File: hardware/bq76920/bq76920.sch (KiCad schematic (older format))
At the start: 10 parts, among them J1 BAT+, J2 Conn_01x06, J3 therm, J4 boot_switch, J5 BAT-, J6 PACK+, J7 PACK-, J8 mcu interface

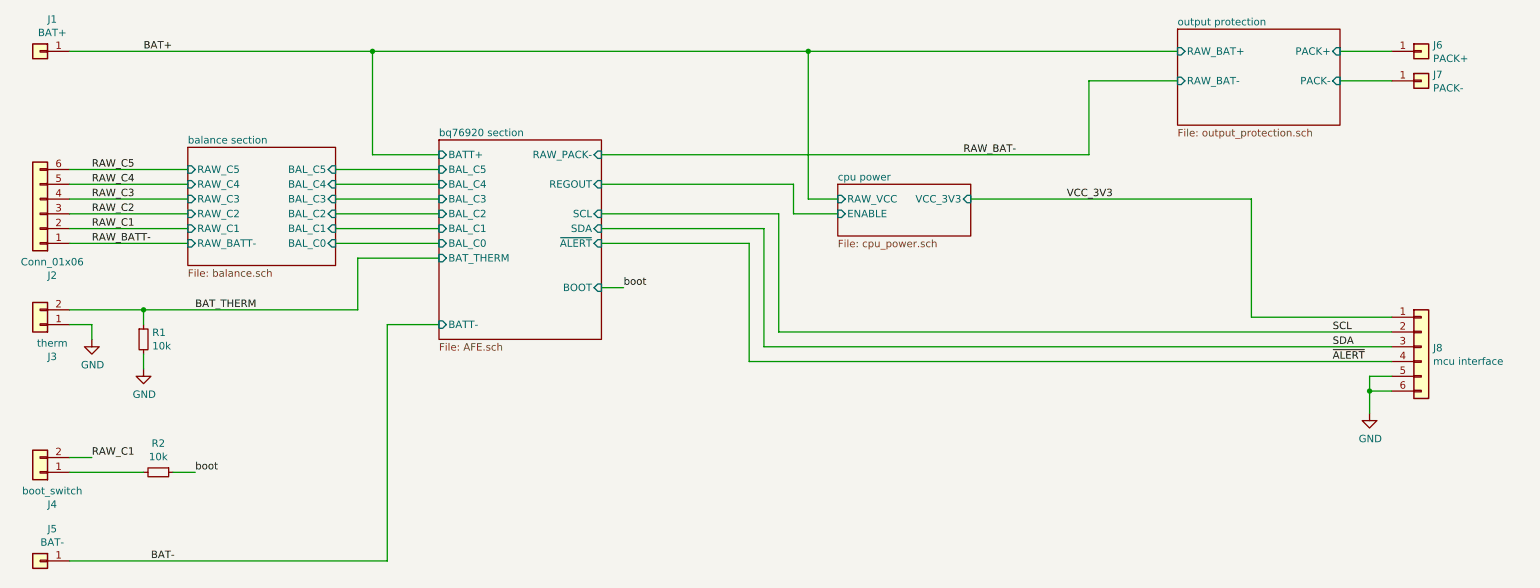
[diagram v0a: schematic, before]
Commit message: remove old project data
Signed-off-by: Ene Alexandru <ene.alexandru@gmail.com>
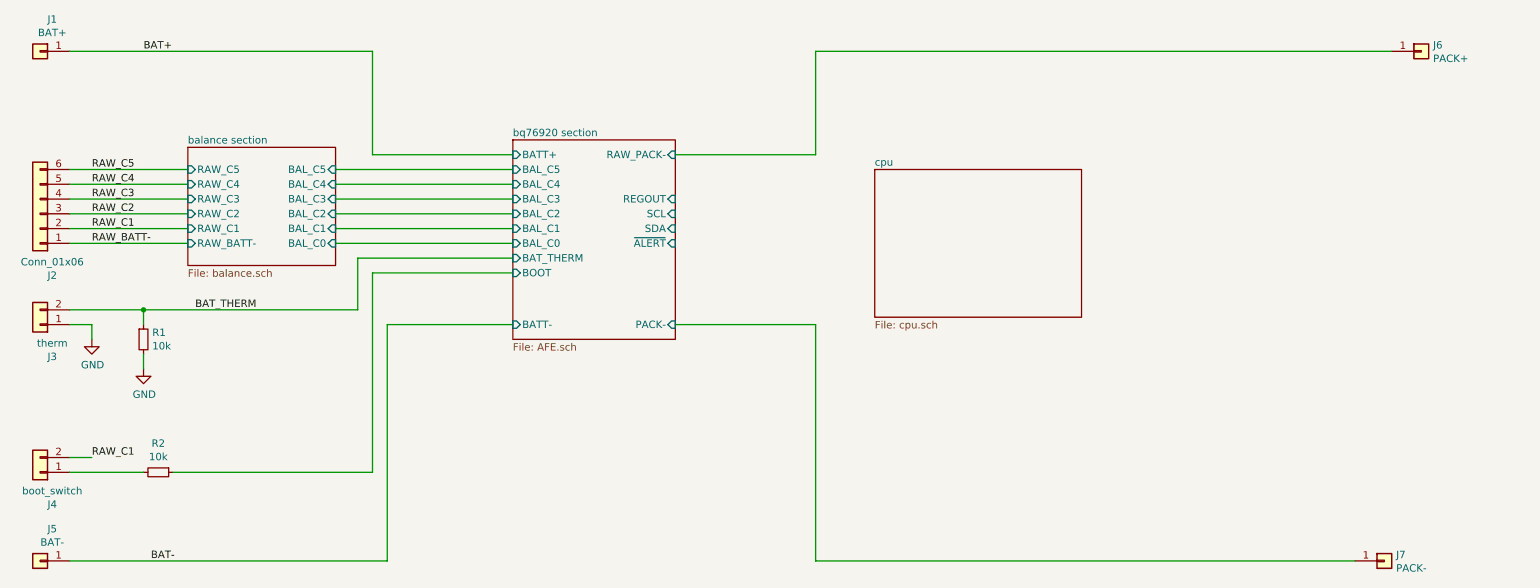
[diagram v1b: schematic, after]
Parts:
- removed J8: mcu interface, Connector_JST:JST_PH_B6B-PH-K_1x06_P2.00mm_Vertical, symbol Connector_Generic:Conn_01x06
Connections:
- net boot renamed bq76920 section/BOOT
- net output protection/PACK+ renamed bq76920 section/RAW_PACK-
- net output protection/PACK- renamed bq76920 section/PACK-
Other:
- moved on the sheet: J7
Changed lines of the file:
@@
 $Descr A4 11693 8268
 encoding utf-8
-Sheet 1 5
+Sheet 1 4
 Title ""
 Date ""
@@
 $EndDescr
 $Sheet
-S 3500 1500 1100 1350
+S 4000 1500 1100 1350
 U 5D32E153
 F0 "bq76920 section" 50
 F1 "AFE.sch" 50
-F2 "BAL_C5" I L 3500 1700 50
-F3 "BAL_C4" I L 3500 1800 50
-F4 "BAL_C3" I L 3500 1900 50
-F5 "BAL_C2" I L 3500 2000 50
-F6 "BAL_C1" I L 3500 2100 50
-F7 "BAL_C0" I L 3500 2200 50
-F8 "BATT-" I L 3500 2750 50
-F9 "~ALERT" I R 4600 2200 50
-F10 "BATT+" I L 3500 1600 50
-F11 "SCL" I R 4600 2000 50
-F12 "SDA" I R 4600 2100 50
-F13 "BOOT" I R 4600 2500 50
-F14 "BAT_THERM" I L 3500 2300 50
-F15 "REGOUT" I R 4600 1800 50
-F16 "RAW_PACK-" I R 4600 1600 50
+F2 "BAL_C5" I L 4000 1700 50
+F3 "BAL_C4" I L 4000 1800 50
+F4 "BAL_C3" I L 4000 1900 50
+F5 "BAL_C2" I L 4000 2000 50
+F6 "BAL_C1" I L 4000 2100 50
+F7 "BAL_C0" I L 4000 2200 50
+F8 "BATT-" I L 4000 2750 50
+F9 "~ALERT" I R 5100 2200 50
+F10 "BATT+" I L 4000 1600 50
+F11 "SCL" I R 5100 2000 50
+F12 "SDA" I R 5100 2100 50
+F13 "BOOT" I L 4000 2400 50
+F14 "BAT_THERM" I L 4000 2300 50
+F15 "REGOUT" I R 5100 1900 50
+F16 "RAW_PACK-" I R 5100 1600 50
+F17 "PACK-" I R 5100 2750 50
 $EndSheet
 $Sheet
@@
 	-1   0    0    -1
 $EndComp
-Wire Wire Line
-	2800 1700 3500 1700
-Wire Wire Line
-	3500 1800 2800 1800
-Wire Wire Line
-	2800 1900 3500 1900
-Wire Wire Line
-	3500 2000 2800 2000
-Wire Wire Line
-	2800 2100 3500 2100
-Wire Wire Line
-	3500 2200 2800 2200
 $Comp
 L Connector_Generic:Conn_01x02 J3
@@
 Wire Wire Line
 	2950 2300 2950 2650
-Wire Wire Line
-	2950 2300 3500 2300
-Wire Wire Line
-	3150 2750 3500 2750
-$Sheet
-S 8500 750  1100 650
-U 5D5964BC
-F0 "output protection" 50
-F1 "output_protection.sch" 50
-F2 "RAW_BAT+" I L 8500 900 50
-F3 "RAW_BAT-" I L 8500 1100 50
-F4 "PACK+" I R 9600 900 50
-F5 "PACK-" I R 9600 1100 50
-$EndSheet
 $Comp
 L Connector_Generic:Conn_01x01 J6
@@
 L Connector_Generic:Conn_01x01 J7
 U 1 1 5D59CAFF
-P 10150 1100
-F 0 "J7" H 10230 1142 50  0000 L CNN
-F 1 "PACK-" H 10230 1051 50  0000 L CNN
-F 2 "bq76920:power_pin" H 10150 1100 50  0001 C CNN
-F 3 "~" H 10150 1100 50  0001 C CNN
-	1    10150 1100
-	1    0    0    -1
-$EndComp
-Wire Wire Line
-	9600 900  9950 900
-$Sheet
-S 6200 1800 900  350
-U 5D59E152
-F0 "cpu power" 50
-F1 "cpu_power.sch" 50
-F2 "ENABLE" I L 6200 2000 50
-F3 "RAW_VCC" I L 6200 1900 50
-F4 "VCC_3V3" I R 7100 1900 50
-$EndSheet
-Wire Wire Line
-	9950 1100 9600 1100
+P 9900 4350
+F 0 "J7" H 9980 4392 50  0000 L CNN
+F 1 "PACK-" H 9980 4301 50  0000 L CNN
+F 2 "bq76920:power_pin" H 9900 4350 50  0001 C CNN
+F 3 "~" H 9900 4350 50  0001 C CNN
+	1    9900 4350
+	1    0    0    -1
+$EndComp
 Wire Wire Line
 	1000 900  3050 900
-Wire Wire Line
-	7900 1600 7900 1100
-Wire Wire Line
-	7900 1100 8500 1100
-Wire Wire Line
-	4600 1600 7900 1600
-Wire Wire Line
-	6200 1900 6000 1900
-Wire Wire Line
-	6000 1900 6000 900
-Connection ~ 6000 900
-Wire Wire Line
-	6000 900  8500 900
-Wire Wire Line
-	4600 1800 5900 1800
-Wire Wire Line
-	5900 1800 5900 2000
-Wire Wire Line
-	5900 2000 6200 2000
-Wire Wire Line
-	3150 2750 3150 4350
 $Comp
 L Device:R_Small R1
@@
 	-1   0    0    1
 $EndComp
-Text Label 4750 2500 0    50   ~ 0
-boot
-Wire Wire Line
-	4750 2500 4600 2500
-Text Label 1850 3750 0    50   ~ 0
-boot
 Text Label 1150 2100 0    50   ~ 0
 RAW_C1
@@
 $EndComp
 Wire Wire Line
-	1700 3750 1850 3750
-Wire Wire Line
 	1000 3750 1500 3750
-$Comp
-L Connector_Generic:Conn_01x06 J8
-U 1 1 5D5E72CD
-P 10150 2900
-F 0 "J8" H 10230 2892 50  0000 L CNN
-F 1 "mcu interface" H 10230 2801 50  0000 L CNN
-F 2 "Connector_JST:JST_PH_B6B-PH-K_1x06_P2.00mm_Vertical" H 10150 2900 50  0001 C CNN
-F 3 "~" H 10150 2900 50  0001 C CNN
-	1    10150 2900
-	1    0    0    -1
-$EndComp
-Wire Wire Line
-	9950 2700 9000 2700
-Wire Wire Line
-	9000 2700 9000 1900
-Wire Wire Line
-	9000 1900 7100 1900
-Wire Wire Line
-	4600 2000 5800 2000
-Wire Wire Line
-	5800 2000 5800 2800
-Wire Wire Line
-	5800 2800 9950 2800
-Wire Wire Line
-	9950 2900 5700 2900
-Wire Wire Line
-	5700 2900 5700 2100
-Wire Wire Line
-	5700 2100 4600 2100
-Wire Wire Line
-	9950 3000 5600 3000
-Wire Wire Line
-	5600 3000 5600 2200
-Wire Wire Line
-	5600 2200 4600 2200
-$Comp
-L power:GND #PWR03
-U 1 1 5D5EC925
-P 9800 3350
-F 0 "#PWR03" H 9800 3100 50  0001 C CNN
-F 1 "GND" H 9805 3177 50  0000 C CNN
-F 2 "" H 9800 3350 50  0001 C CNN
-F 3 "" H 9800 3350 50  0001 C CNN
-	1    9800 3350
-	1    0    0    -1
-$EndComp
-Wire Wire Line
-	9800 3350 9800 3200
-Wire Wire Line
-	9800 3100 9950 3100
-Wire Wire Line
-	9950 3200 9800 3200
-Connection ~ 9800 3200
-Wire Wire Line
-	9800 3200 9800 3100
 Wire Wire Line
 	1000 4350 3150 4350
 Wire Wire Line
-	3500 1600 3050 1600
-Wire Wire Line
 	3050 1600 3050 900
-Connection ~ 3050 900
-Wire Wire Line
-	3050 900  6000 900
 Text Label 1500 900  0    50   ~ 0
 BAT+
@@
 Text Label 1550 4350 0    50   ~ 0
 BAT-
-Text Label 7050 1600 0    50   ~ 0
-RAW_BAT-
-Text Label 7750 1900 0    50   ~ 0
-VCC_3V3
-Text Label 9550 2800 0    50   ~ 0
-SCL
-Text Label 9550 2900 0    50   ~ 0
-SDA
-Text Label 9550 3000 0    50   ~ 0
-~ALERT
+Wire Wire Line
+	3050 1600 4000 1600
+Wire Wire Line
+	2800 1700 4000 1700
+Wire Wire Line
+	2800 1800 4000 1800
+Wire Wire Line
+	2800 1900 4000 1900
+Wire Wire Line
+	2800 2000 4000 2000
+Wire Wire Line
+	2800 2100 4000 2100
+Wire Wire Line
+	2800 2200 4000 2200
+Wire Wire Line
+	2950 2300 4000 2300
+Wire Wire Line
+	3050 3750 3050 2400
+Wire Wire Line
+	3050 2400 4000 2400
+Wire Wire Line
+	1700 3750 3050 3750
+Wire Wire Line
+	4000 2750 3150 2750
+Wire Wire Line
+	3150 2750 3150 4350
+Wire Wire Line
+	5100 1600 6050 1600
+Wire Wire Line
+	6050 1600 6050 900
+Wire Wire Line
+	6050 900  9950 900
+Wire Wire Line
+	5100 2750 6050 2750
+Wire Wire Line
+	6050 2750 6050 4350
+Wire Wire Line
+	6050 4350 9700 4350
+$Sheet
+S 6450 1700 1400 1000
+U 5E142913
+F0 "cpu" 50
+F1 "cpu.sch" 50
+$EndSheet
 $EndSCHEMATC

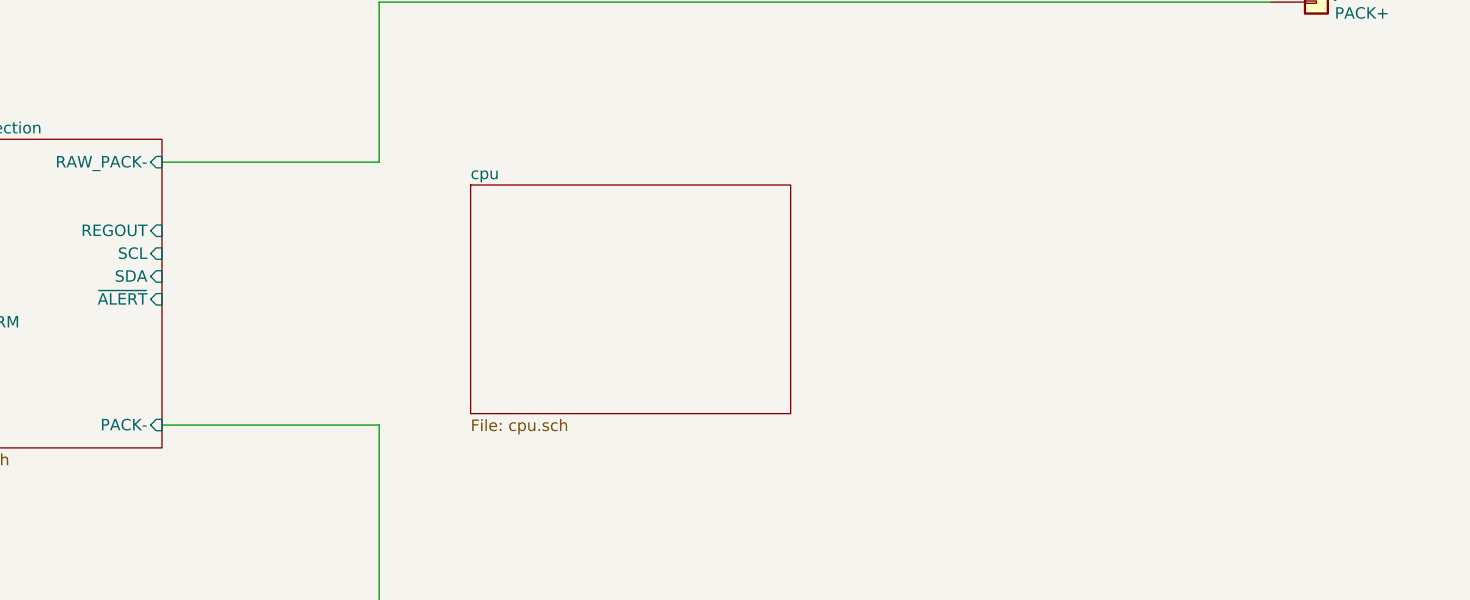
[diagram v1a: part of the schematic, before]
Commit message: update cpu and reduce BOM
Signed-off-by: Ene Alexandru <ene.alexandru@gmail.com>
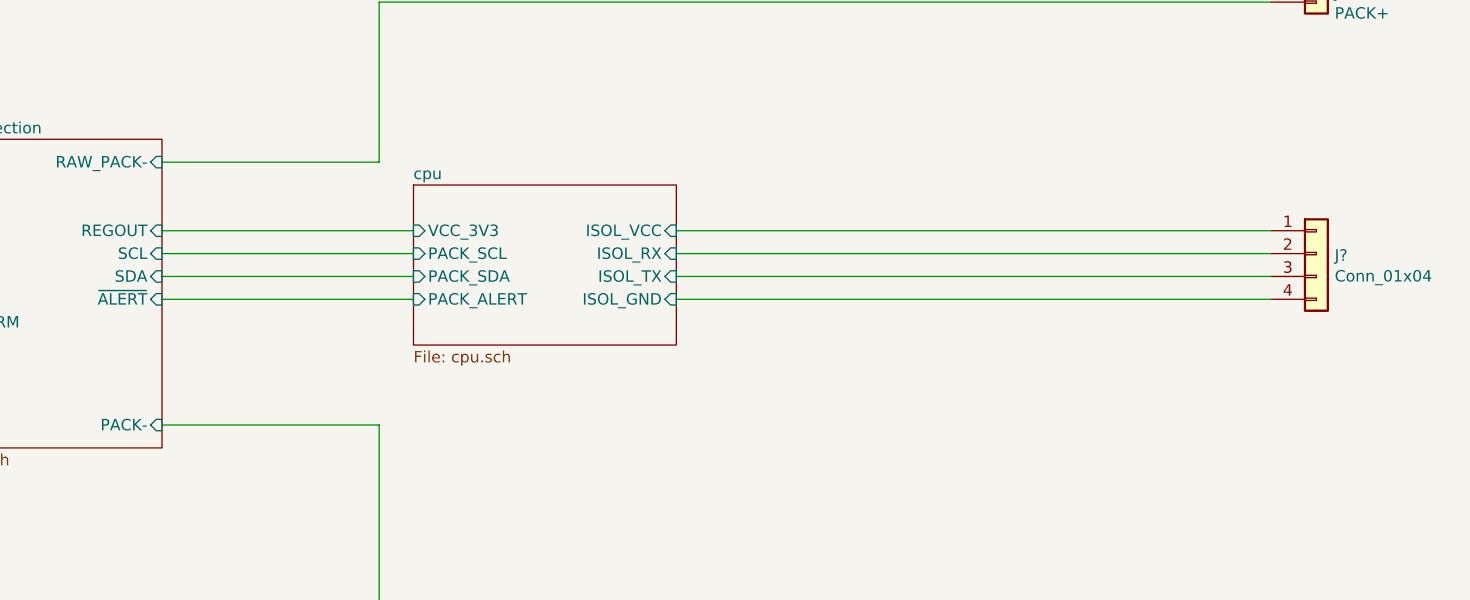
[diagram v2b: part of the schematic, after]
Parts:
- added J?: Conn_01x04, symbol Connector_Generic:Conn_01x04
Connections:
- new net cpu/ISOL_GND: J?.4 (Pin_4)
- new net cpu/ISOL_RX: J?.2 (Pin_2)
- new net cpu/ISOL_TX: J?.3 (Pin_3)
- new net cpu/ISOL_VCC: J?.1 (Pin_1)
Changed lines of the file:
@@
 	6050 4350 9700 4350
 $Sheet
-S 6450 1700 1400 1000
+S 6200 1700 1150 700
 U 5E142913
 F0 "cpu" 50
 F1 "cpu.sch" 50
+F2 "VCC_3V3" I L 6200 1900 50
+F3 "PACK_SCL" I L 6200 2000 50
+F4 "PACK_SDA" I L 6200 2100 50
+F5 "PACK_ALERT" I L 6200 2200 50
+F6 "ISOL_VCC" I R 7350 1900 50
+F7 "ISOL_RX" I R 7350 2000 50
+F8 "ISOL_TX" I R 7350 2100 50
+F9 "ISOL_GND" I R 7350 2200 50
 $EndSheet
+Wire Wire Line
+	6200 1900 5100 1900
+Wire Wire Line
+	5100 2000 6200 2000
+Wire Wire Line
+	6200 2100 5100 2100
+Wire Wire Line
+	5100 2200 6200 2200
+$Comp
+L Connector_Generic:Conn_01x04 J?
+U 1 1 5E14DD4B
+P 10150 2000
+F 0 "J?" H 10230 1992 50  0000 L CNN
+F 1 "Conn_01x04" H 10230 1901 50  0000 L CNN
+F 2 "" H 10150 2000 50  0001 C CNN
+F 3 "~" H 10150 2000 50  0001 C CNN
+	1    10150 2000
+	1    0    0    -1
+$EndComp
+Wire Wire Line
+	9950 1900 7350 1900
+Wire Wire Line
+	7350 2000 9950 2000
+Wire Wire Line
+	9950 2100 7350 2100
+Wire Wire Line
+	7350 2200 9950 2200
 $EndSCHEMATC
